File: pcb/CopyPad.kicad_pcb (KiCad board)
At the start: 2 copper layers, 61.2 x 65.6 mm, 9 parts, among them J1 OLED_128x32, SW1 SW_Push, SW2 SW_Push, SW3 SW_Push, SW4 RotaryEncoder_Switch, U1 XIAO-RP2040-DIP

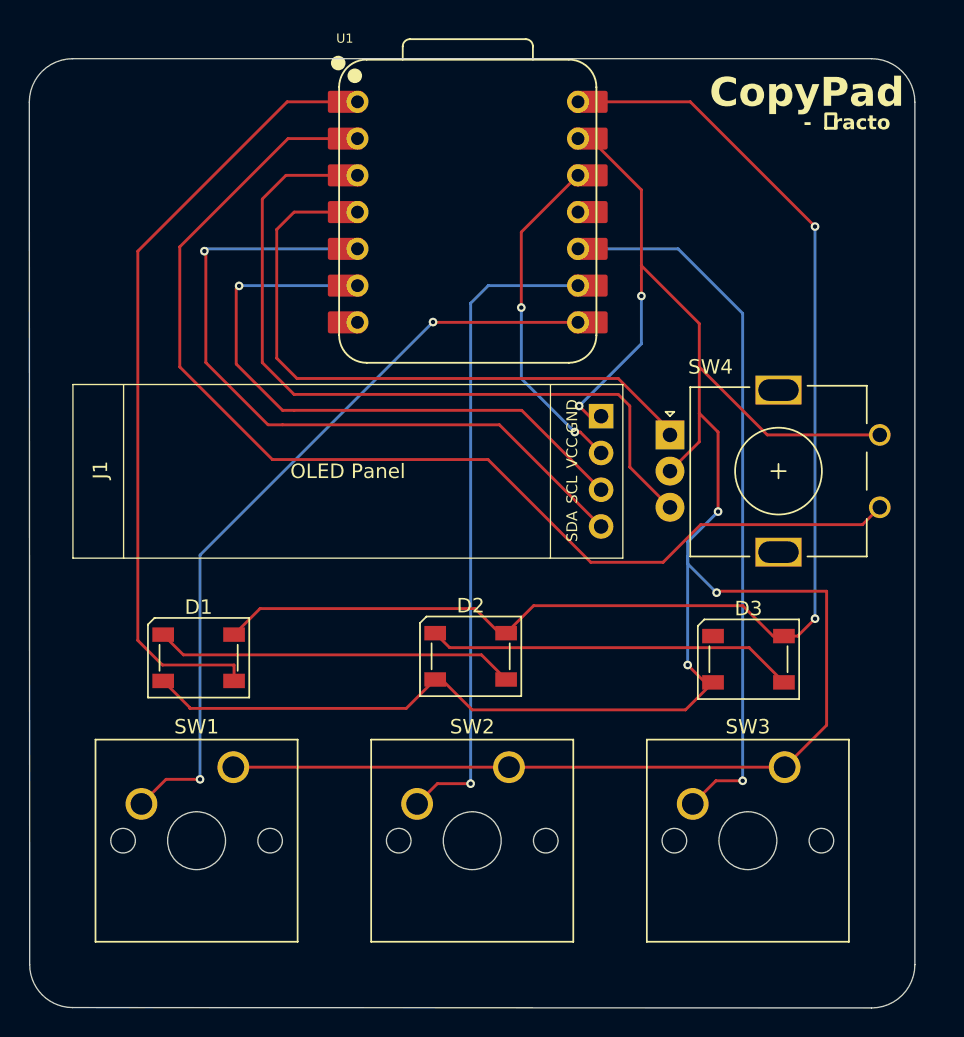
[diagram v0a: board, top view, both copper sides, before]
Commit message: update to replace SK6812 with SK6812 MINI
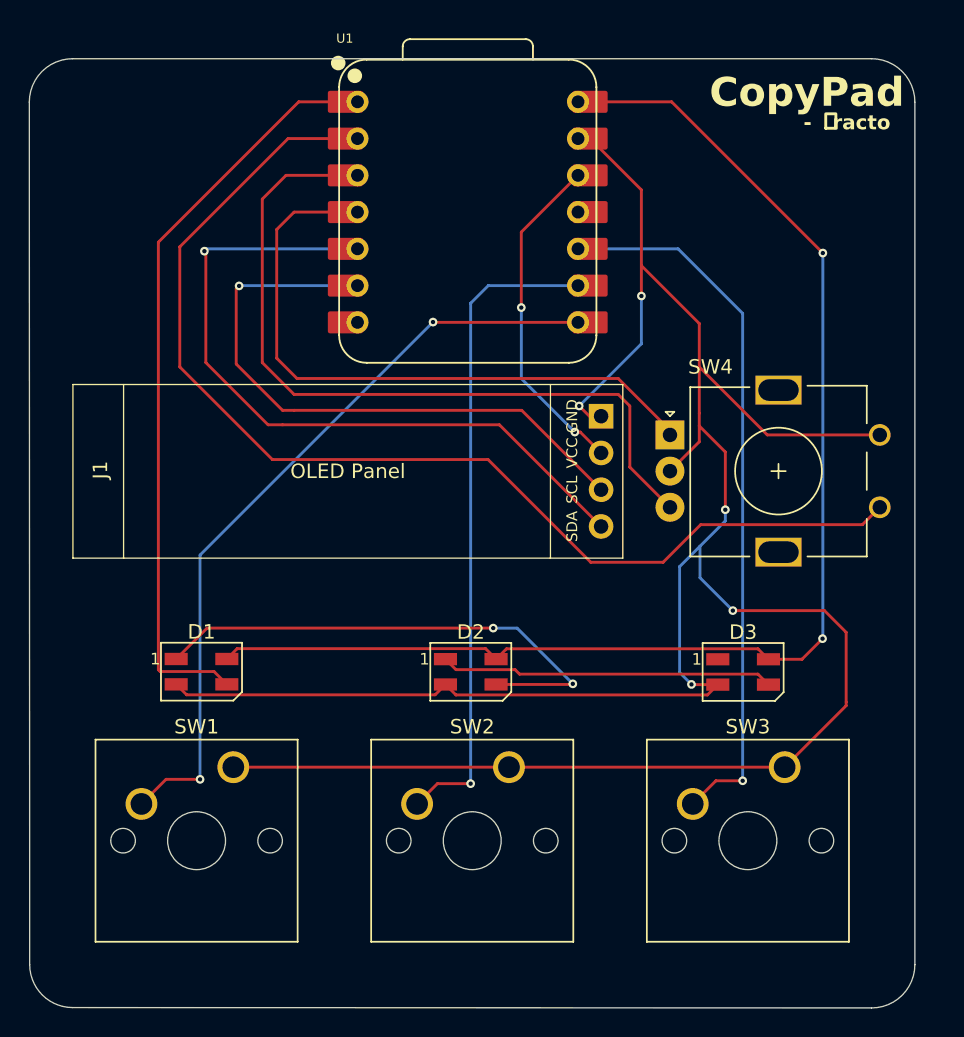
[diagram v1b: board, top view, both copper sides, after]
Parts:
- D1, D2, D3: value SK6812 -> SK6812MINI; footprint LED_SMD:LED_SK6812_PLCC4_5.0x5.0mm_P3.2mm -> LED_SMD:LED_SK6812MINI_PLCC4_3.5x3.5mm_P1.75mm
- moved D2 1.07 mm to (136.4, 105.4)
- moved D1 0.98 mm to (117.8, 105.4)
- moved D3 0.95 mm to (155.2, 105.4)
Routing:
- net Net-(D1-DOUT): track 25.0 -> 35.2 mm, vias 0 -> 2
- net Net-(D2-DOUT): track 25.5 -> 23.0 mm
- net Net-(D1-DIN): track 54.8 -> 52.5 mm
- net Net-(U1-GPIO28/ADC2/A2): track 52.5 -> 53.4 mm
